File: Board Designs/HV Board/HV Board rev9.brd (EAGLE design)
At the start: 118.6 x 71.4 mm, 60 parts, among them IC1 OKI-78SR, IC2 NE5532SOIC

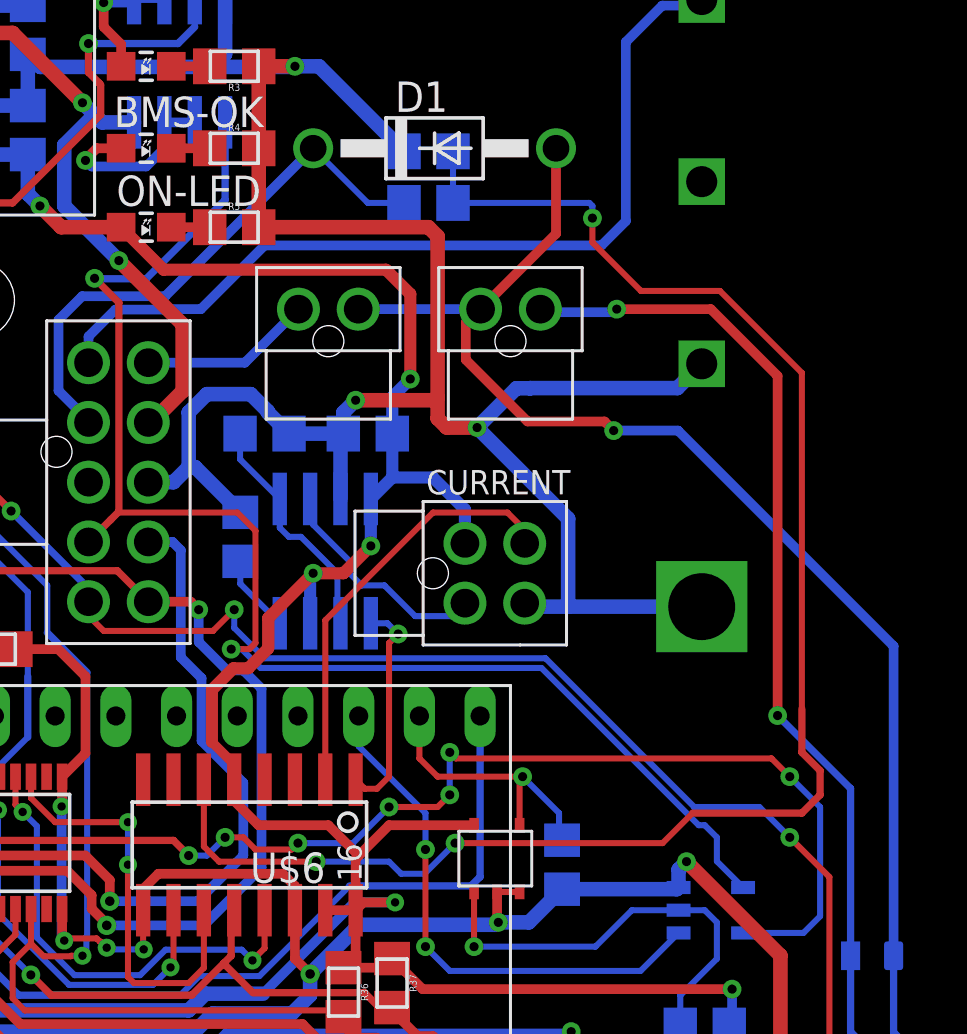
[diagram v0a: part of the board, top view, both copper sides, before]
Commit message: Prep silkscreen and dimensions for manufacture
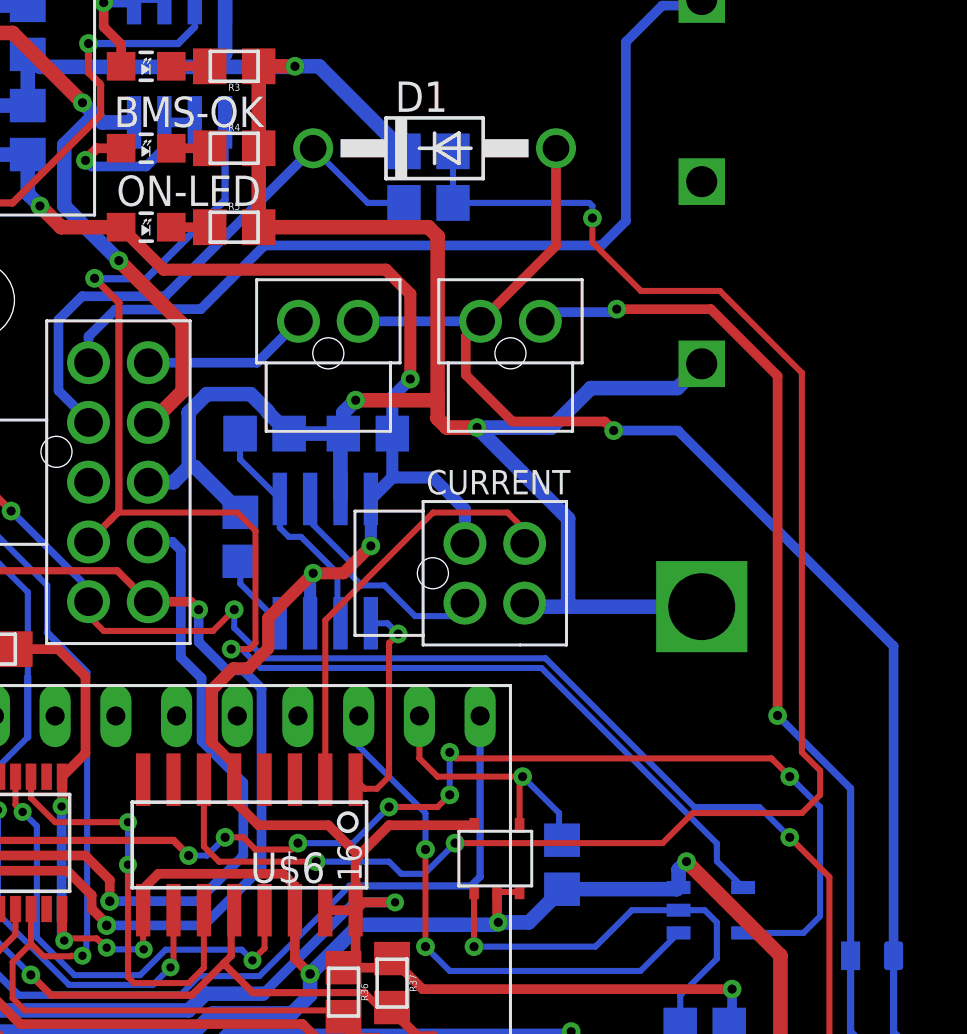
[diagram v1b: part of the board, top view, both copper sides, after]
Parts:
- moved INTERLOCK 0.51 mm to (29.2, 34.5)
- moved RELAYS 0.51 mm to (36.8, 34.5)

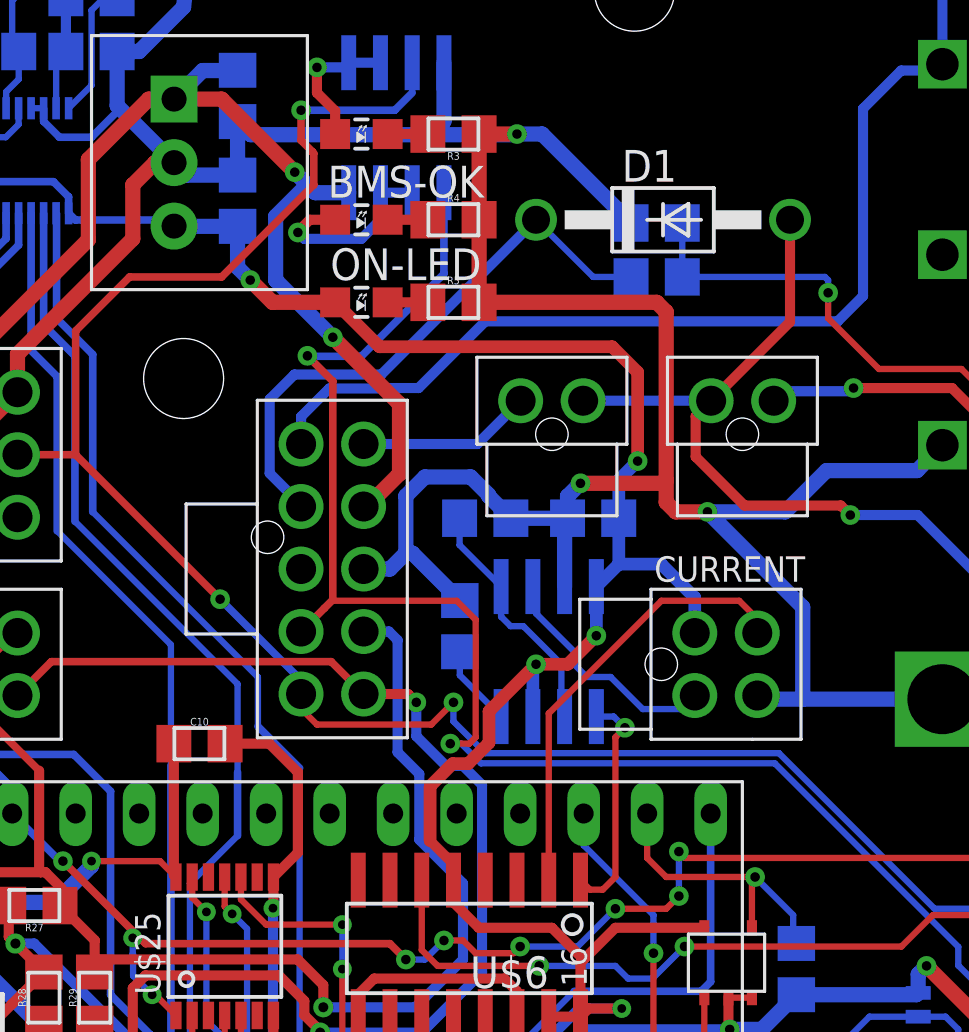
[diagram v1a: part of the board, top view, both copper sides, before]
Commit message: Silkscreen modifications, small adjustments to trace locations
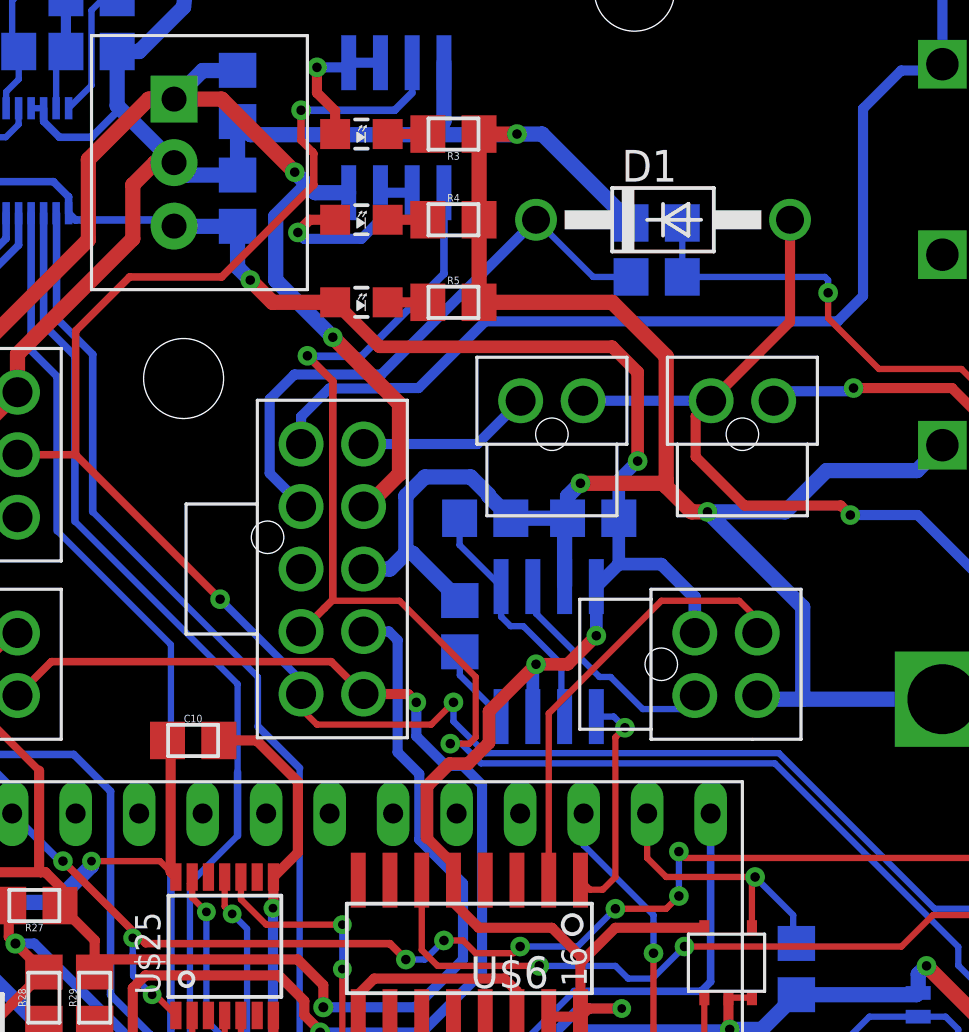
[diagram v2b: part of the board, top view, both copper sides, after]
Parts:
- moved C10 0.28 mm to (14.9, 21.0)
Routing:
- net BMS_OK: track 60.4 -> 59.0 mm
- net GND: track 269.3 -> 268.0 mm
